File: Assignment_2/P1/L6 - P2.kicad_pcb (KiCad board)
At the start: 2 copper layers, 82 x 43 mm, 30 parts, among them J1 Conn_01x06_Socket, SW1 SW_SPDT_312, SW2 SW_SPDT_312, U1 ATtiny45-20P

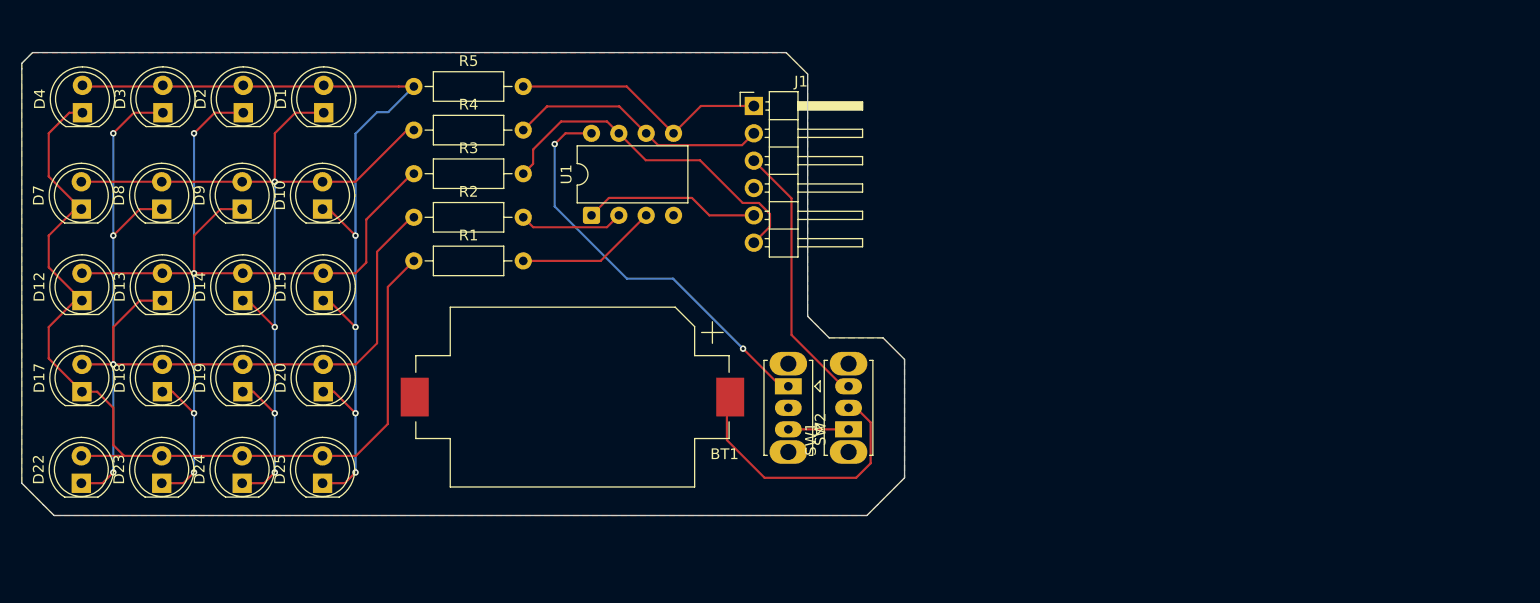
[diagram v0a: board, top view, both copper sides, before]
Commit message: Update layout of all assignments
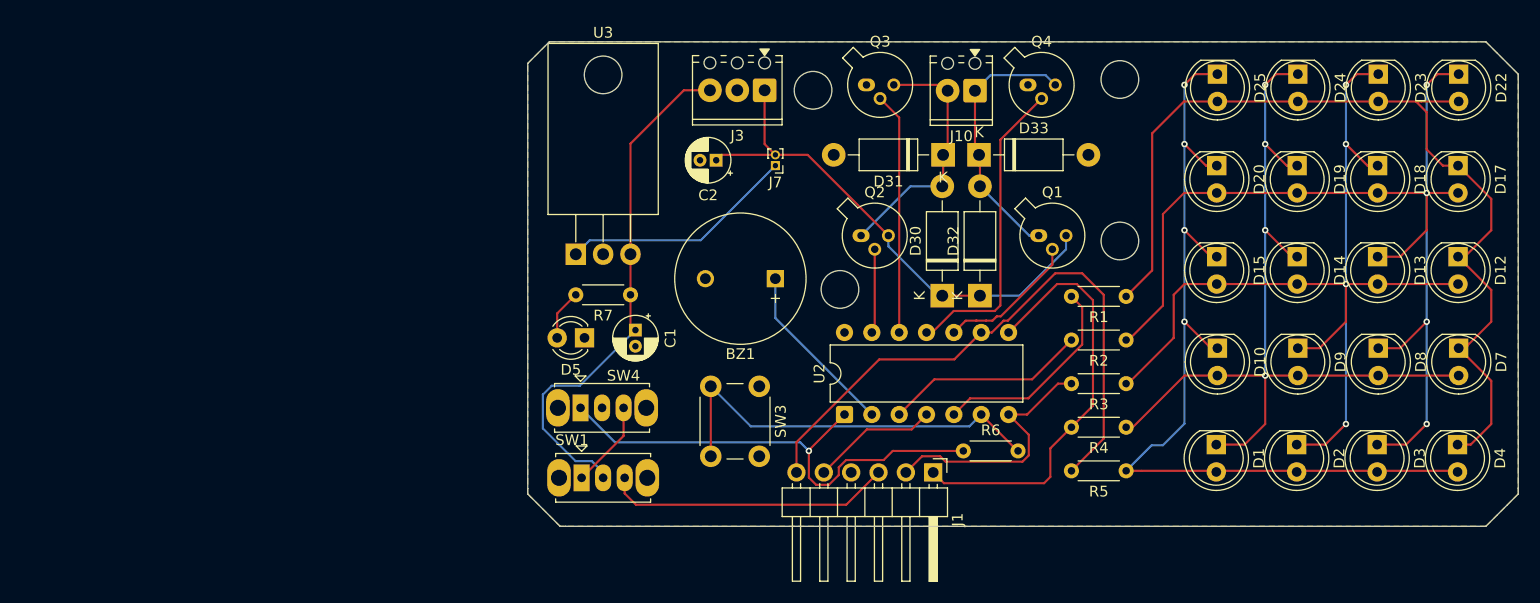
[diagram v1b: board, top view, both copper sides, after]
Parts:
- removed BT1: Battery, Battery:BatteryHolder_Keystone_1060_1x2032
- removed SW2: SW_SPDT_312, Button_Switch_THT:SW_Slide_SPDT_Straight_CK_OS102011MS2Q
- removed U1: ATtiny45-20P, Package_DIP:DIP-8_W7.62mm
- added BZ1: Buzzer, Buzzer_Beeper:MagneticBuzzer_ProSignal_ABT-410-RC, F.Cu at (132.0, 57.5)
- added C1: C_Polarized_Small, Capacitor_THT:CP_Radial_D4.0mm_P1.50mm, F.Cu at (119.0, 62.3)
- added C2: C_Polarized_Small, Capacitor_THT:CP_Radial_D4.0mm_P1.50mm, F.Cu at (126.5, 46.5)
- added D30: 1N4007, Diode_THT:D_DO-41_SOD81_P10.16mm_Horizontal, F.Cu at (147.5, 59.1)
- added D31: 1N4007, Diode_THT:D_DO-41_SOD81_P10.16mm_Horizontal, F.Cu at (147.6, 46.0)
- added D32: 1N4007, Diode_THT:D_DO-41_SOD81_P10.16mm_Horizontal, F.Cu at (151.0, 59.1)
- added D33: 1N4007, Diode_THT:D_DO-41_SOD81_P10.16mm_Horizontal, F.Cu at (150.9, 46.0)
- added D5: LED, LED_THT:LED_D3.0mm, F.Cu at (114.3, 63.0)
- added J10: Screw_Terminal_01x02, TerminalBlock_Phoenix:TerminalBlock_Phoenix_MPT-0,5-2-2.54_1x02_P2.54mm_Horizontal, F.Cu at (150.5, 40.0)
- added J3: Screw_Terminal_01x03, TerminalBlock_Phoenix:TerminalBlock_Phoenix_MPT-0,5-3-2.54_1x03_P2.54mm_Horizontal, F.Cu at (131.0, 40.0)
- added J7: Conn_01x02_Pin, Connector_PinHeader_1.00mm:PinHeader_1x02_P1.00mm_Vertical, F.Cu at (132.0, 47.0)
- added Q1: BC107, Package_TO_SOT_THT:TO-18-3, F.Cu at (156.5, 53.5)
- added Q2: BC107, Package_TO_SOT_THT:TO-18-3, F.Cu at (140.0, 53.5)
- added Q3: BC107, Package_TO_SOT_THT:TO-18-3, F.Cu at (140.5, 39.5)
- added Q4: BC107, Package_TO_SOT_THT:TO-18-3, F.Cu at (155.5, 39.5)
- added R6: R, Resistor_THT:R_Axial_DIN0204_L3.6mm_D1.6mm_P5.08mm_Horizontal, F.Cu at (149.5, 73.5)
- added R7: R, Resistor_THT:R_Axial_DIN0204_L3.6mm_D1.6mm_P5.08mm_Horizontal, F.Cu at (118.5, 59.0)
- added SW3: SW_DPST_x2, Button_Switch_THT:SW_PUSH_6mm_H5mm, F.Cu at (130.5, 67.5)
- added SW4: SW_SPDT_312, Button_Switch_THT:SW_Slide_SPDT_Straight_CK_OS102011MS2Q, F.Cu at (113.9, 69.5)
- added U2: ATtiny84A-P, Package_DIP:DIP-14_W7.62mm, F.Cu at (138.4, 70.1)
- added U3: LM7805_TO220, Package_TO_SOT_THT:TO-220-3_Horizontal_TabDown, F.Cu at (113.5, 55.2)
- R1, R2, R3, R4, R5: footprint Resistor_THT:R_Axial_DIN0207_L6.3mm_D2.5mm_P10.16mm_Horizontal -> Resistor_THT:R_Axial_DIN0204_L3.6mm_D1.6mm_P5.08mm_Horizontal
- moved D22 133.5 mm to (195.5, 38.5), turned to -90 degrees
- moved D4 131.4 mm to (195.4, 72.9), turned to -90 degrees
- moved D17 129.5 mm to (195.4, 47.0), turned to -90 degrees
- moved D7 128.6 mm to (195.5, 64.0), turned to -90 degrees
- moved D12 127.9 mm to (195.4, 55.5), turned to -90 degrees
- moved D23 119.2 mm to (188.0, 38.5), turned to -90 degrees
- moved D3 116.9 mm to (187.9, 72.9), turned to -90 degrees
- moved D18 114.8 mm to (187.9, 47.0), turned to -90 degrees
- moved D8 113.7 mm to (188.0, 64.0), turned to -90 degrees
- moved D13 113.0 mm to (187.9, 55.5), turned to -90 degrees
- moved D24 105.2 mm to (180.5, 38.5), turned to -90 degrees
- moved D2 102.6 mm to (180.4, 72.9), turned to -90 degrees
- moved D19 100.2 mm to (180.5, 47.0), turned to -90 degrees
- moved D9 98.9 mm to (180.5, 64.0), turned to -90 degrees
- moved D14 98.0 mm to (180.5, 55.5), turned to -90 degrees
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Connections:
- J1 pad 6: SCK -> Matrix1
- R1 pad 2: Net-(U1-XTAL2/PB4) -> Matrix5
- R2 pad 2: Net-(U1-XTAL1/PB3) -> Matrix4
- R3 pad 2: SCK -> MOSI
- R4 pad 2: MOSI -> MISO
- R5 pad 2: MISO -> Matrix1
- SW1 pad 2: BAT-VCC -> TERMINAL-VCC
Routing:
- net Matrix1: track 0.00 -> 56.3 mm
- net TERMINAL-VCC: track 0.00 -> 49.0 mm
- net Vs: track 0.00 -> 48.2 mm
- net Switch_Input: track 0.00 -> 38.4 mm
- net SCK: track 32.6 -> 0.00 mm
- net M3: track 0.00 -> 28.7 mm
- net BAT-VCC: track 25.9 -> 0.00 mm
- net Net-(D32-A): track 0.00 -> 25.6 mm
- net Net-(D30-A): track 0.00 -> 25.3 mm
- net M2: track 0.00 -> 22.5 mm
- net Net-(J7-Pin_1): track 0.00 -> 21.9 mm
- net Matrix5: track 0.00 -> 19.5 mm
- net Matrix4: track 0.00 -> 18.9 mm
- net Buzz_Output: track 0.00 -> 16.3 mm
- net MISO: track 24.3 -> 39.9 mm
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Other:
- board size 82 x 43 mm -> 92 x 45 mm

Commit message: Update layout of all assignments - P2
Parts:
- added G***: LOGO, Logo:logo, B.Cu at (117.0, 46.0)
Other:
- board text added: "Name: Ahmed Atef Nasr ID: 1471804251201"
